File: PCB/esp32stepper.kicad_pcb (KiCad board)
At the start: 4 copper layers, 100 x 80 mm, 117 parts, among them J1 Conn_01x02_Pin, J4 spare, J5 UART0 DEBUG, U1 ESP32-S3-WROOM-2, U2 LDL1117_SOT223, U3 LT8610, U4 74HC595D, U5 USBLC6-2SC6, U6 TCA9548APWR

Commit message: pcb version ready for final check
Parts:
- added ?: , , F.Cu at (200.4, 164.2)
- added ?: , , F.Cu at (198.0, 169.6)
- added ?: , , F.Cu at (190.3, 161.2)
- added ?: , , F.Cu at (198.0, 164.2)
- added ?: , , F.Cu at (205.4, 164.2)
- added ?: , , F.Cu at (200.4, 161.2)
- added ?: , , F.Cu at (190.3, 169.6)
- added ?: , , F.Cu at (198.0, 166.6)
- added ?: , , F.Cu at (190.3, 153.6)
- added ?: , , F.Cu at (198.0, 161.2)
- added ?: , , F.Cu at (200.4, 166.6)
- added ?: , , F.Cu at (200.4, 169.6)
- added ?: , , F.Cu at (202.8, 161.2)
- added ?: , , F.Cu at (202.8, 164.2)
- added C25: 100uF/50V, Capacitor_SMD:CP_Elec_8x10.5, F.Cu at (166.7, 110.5)
- added C26: 100uF/50V, Capacitor_SMD:CP_Elec_8x10.5, F.Cu at (189.6, 110.6)
- added C27: 100uF/50V, Capacitor_SMD:CP_Elec_8x10.5, F.Cu at (215.0, 110.1)
- added C28: 100uF/50V, Capacitor_SMD:CP_Elec_8x10.5, F.Cu at (236.8, 110.4)
- added J6: PWR_SWITCH, Connector_PinHeader_2.54mm:PinHeader_1x03_P2.54mm_Vertical, F.Cu at (242.6, 138.4)
- added NPN1: BC817-40, Package_TO_SOT_SMD:TSOT-23_HandSoldering, F.Cu at (248.2, 144.8)
- added REF**: IEAP_LOGO, VNfootprints:IEAP_LOGO, F.Cu at (212.6, 138.6)
- added fan1: Conn_01x02_Pin, Connector_PinHeader_2.54mm:PinHeader_1x02_P2.54mm_Vertical, F.Cu at (250.9, 122.2)
- moved L2 208.1 mm to (246.0, 151.2), turned to -90 degrees
- moved C13 205.8 mm to (244.1, 146.4), turned to 0 degrees
- moved LED1 205.7 mm to (250.4, 152.6)
- moved C11 205.3 mm to (243.0, 148.9), turned to -90 degrees
- moved R7 204.8 mm to (250.6, 149.2), turned to 0 degrees
- moved C12 204.6 mm to (244.2, 143.1), turned to 180 degrees
- moved USB1 203.3 mm to (251.1, 159.1), turned to 90 degrees
- moved R12 202.6 mm to (250.5, 150.8), turned to 0 degrees
- moved barreljack1 202.4 mm to (242.3, 130.2), turned to 90 degrees
- moved C14 202.3 mm to (239.9, 150.1), turned to 90 degrees
- moved R10 202.2 mm to (243.9, 144.6), turned to 0 degrees
- moved R9 200.4 mm to (241.7, 142.2)
- moved U3 198.7 mm to (239.1, 146.1), turned to 0 degrees
- moved C15 196.9 mm to (240.1, 142.0)
- moved R1 195.1 mm to (244.1, 163.4), turned to 180 degrees
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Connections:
- C15 pad 2: Net-(U3-PG) -> Net-(NPN1-B)
- D3 pad 2: Net-(D3-A) -> PWRSWITCH_diode
- F2 pad 1: Net-(PMOS1-S) -> Net-(PMOS1-D)
- LED1 pad 1: GND -> Net-(LED1-K)
- PMOS1 pad 1: 24Vin -> Net-(PMOS1-D)
- PMOS1 pad 2: Net-(D3-A) -> PWRSWITCH_gate
- PMOS1 pad 3: Net-(PMOS1-S) -> 24Vin
- R12 pad 1: Net-(U3-PG) -> +3V3
- R18 pad 1: Net-(D3-A) -> PWRSWITCH_diode
- R7 pad 2: Net-(U3-PG) -> Net-(NPN1-B)
- U3 pad 15: Net-(U3-PG) -> Net-(NPN1-B)
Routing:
- net +3V3: track 173.0 -> 82.1 mm, vias 22 -> 26
- net endswitch3: track 37.8 -> 74.6 mm, vias 1 -> 2
- net PWRSWITCH_diode: track 0.00 -> 36.0 mm
- net encoder3_SC: track 64.9 -> 32.6 mm, vias 2 -> 0
- net encoder3_SD: track 67.0 -> 35.7 mm, vias 2 -> 0
- net PWRSWITCH_gate: track 0.00 -> 26.8 mm
- net UART: track 150.5 -> 124.9 mm, vias 4 -> 1
- net 24V: track 27.7 -> 50.2 mm
- net Net-(NPN1-B): track 0.00 -> 21.7 mm
- net rx_ext: track 29.7 -> 10.1 mm, vias 1 -> 0
- net reset: track 32.2 -> 12.9 mm
- net step3: track 76.8 -> 57.9 mm
- net tx_ext: track 29.1 -> 10.4 mm, vias 1 -> 0
- net encoder2_SC: track 36.5 -> 18.5 mm, vias 2 -> 0
- net encoder1_SC: track 20.3 -> 37.9 mm
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- added copper zone on B.Cu, net GND
- added copper zone on F.Cu, net GND
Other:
- board text added: "24vin"
- board text added: "diode"
- board text added: "rx"
- board text added: "tx"

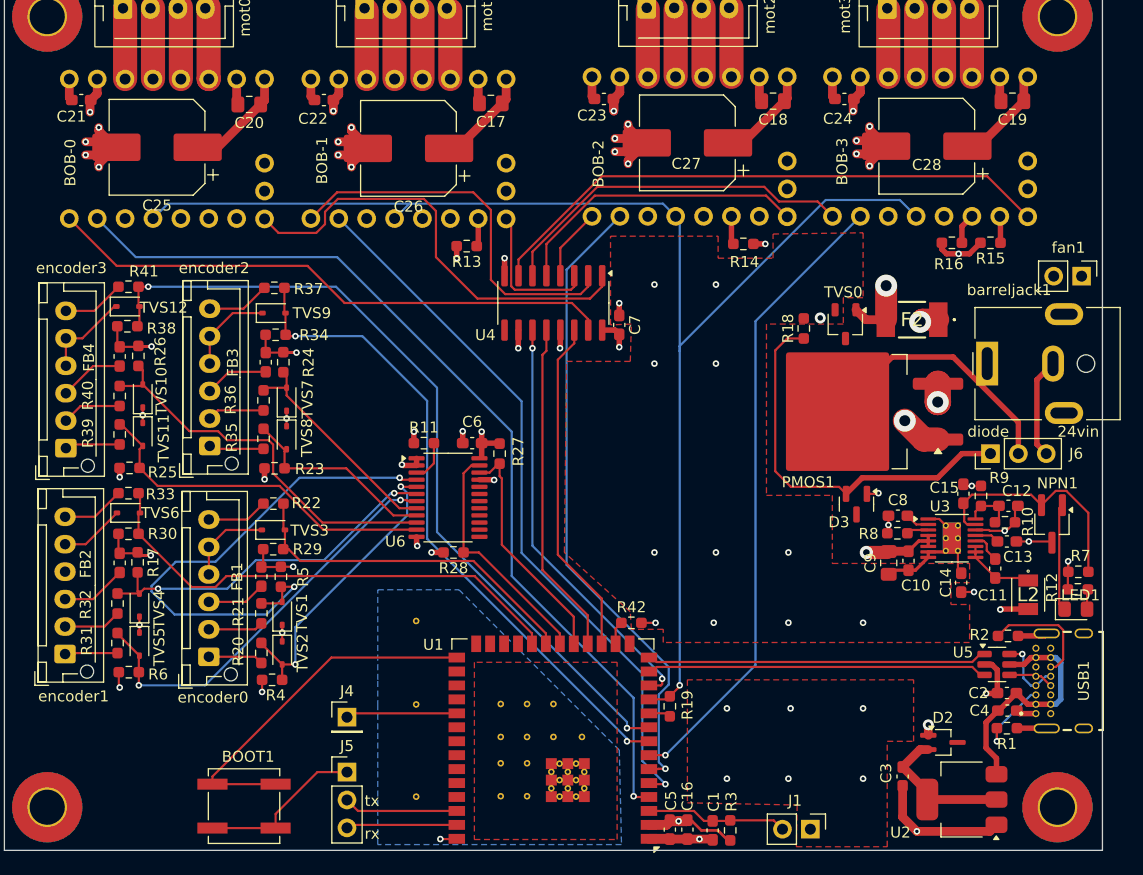
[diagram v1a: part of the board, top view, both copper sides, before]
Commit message: [pcb] Final processing and export of production data
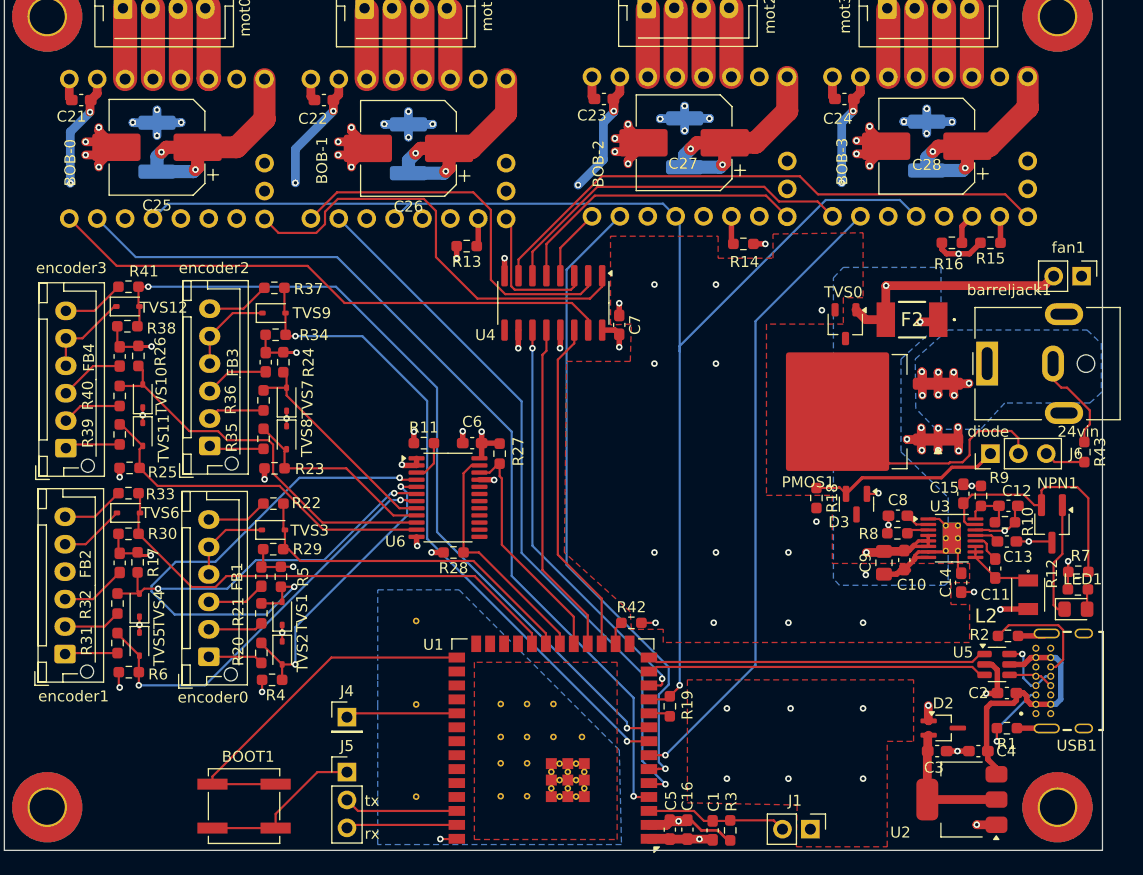
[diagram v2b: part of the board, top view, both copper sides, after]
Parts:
- removed C17, C18, C19, C20: 4u7, Capacitor_SMD:C_0805_2012Metric_Pad1.18x1.45mm_HandSolder
- added F1: Fuse, Fuse:Fuse_1812_4532Metric_Pad1.30x3.40mm_HandSolder, B.Cu at (166.7, 110.5)
- added F3: Fuse, Fuse:Fuse_1812_4532Metric_Pad1.30x3.40mm_HandSolder, B.Cu at (189.6, 110.6)
- added F4: Fuse, Fuse:Fuse_1812_4532Metric_Pad1.30x3.40mm_HandSolder, B.Cu at (214.7, 110.1)
- added F5: Fuse, Fuse:Fuse_1812_4532Metric_Pad1.30x3.40mm_HandSolder, B.Cu at (236.8, 110.4)
- added R43: 100k, Resistor_SMD:R_0603_1608Metric_Pad0.98x0.95mm_HandSolder, F.Cu at (251.1, 138.2)
- moved R18 15.5 mm to (226.7, 142.4), turned to -90 degrees
- moved C4 4.54 mm to (241.5, 165.5), turned to 180 degrees
- moved C3 3.91 mm to (237.7, 165.5), turned to 0 degrees
- moved D2 1.31 mm to (238.3, 163.4)
- moved C9 0.44 mm to (232.9, 148.3)
- moved C10 0.39 mm to (234.7, 148.1)
- moved C27 0.30 mm to (214.7, 110.1)
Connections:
- net Net-(PMOS1-D) renamed 24V_Motor
- BOB-0 pad 16: 24V -> Net-(BOB-0-+VM)
- BOB-1 pad 16: 24V -> Net-(BOB-1-+VM)
- BOB-2 pad 16: 24V -> Net-(BOB-2-+VM)
- BOB-3 pad 16: 24V -> Net-(BOB-3-+VM)
- C25 pad 1: 24V -> Net-(BOB-0-+VM)
- C26 pad 1: 24V -> Net-(BOB-1-+VM)
- C27 pad 1: 24V -> Net-(BOB-2-+VM)
- C28 pad 1: 24V -> Net-(BOB-3-+VM)
- J6 pad 3: 24Vin -> PWRSWITCH_Voltage
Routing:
- net +3V3: track 82.1 -> 112.9 mm, vias 26 -> 30
- net 24V_Motor: track 16.5 -> 41.5 mm, vias 2 -> 24
- net Net-(BOB-0-+VM): track 0.00 -> 21.9 mm, vias 0 -> 2
- net Net-(BOB-3-+VM): track 0.00 -> 21.8 mm, vias 0 -> 2
- net Net-(BOB-1-+VM): track 0.00 -> 21.4 mm, vias 0 -> 2
- net Net-(BOB-2-+VM): track 0.00 -> 20.9 mm, vias 0 -> 2
- net 24V: track 50.2 -> 30.3 mm
- net PWRSWITCH_diode: track 36.0 -> 17.7 mm
- net GND: track 173.7 -> 156.2 mm, vias 52 -> 55
- net PWRSWITCH_Voltage: track 0.00 -> 3.79 mm
- net Net-(NPN1-B): track 21.7 -> 23.5 mm
- net PWRSWITCH_gate: track 26.8 -> 25.1 mm
- net VBUS: track 22.1 -> 23.4 mm
- net /CONN/VO_USB_LDO: track 13.2 -> 12.2 mm
- net Net-(LED1-K): track 9.79 -> 10.6 mm
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- added copper zone on B.Cu, net 24V
- added copper zone on In1.Cu, net 24V_Motor
- added copper zone on B.Cu, net 24Vin
- removed copper zone on In1.Cu, net 24V

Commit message: Auto stash before merge of "main" and "origin/main"
[pcb] Updated main connector and LT8610AC layout
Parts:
- removed ? (x14): , 
- removed REF**: IEAP_LOGO, VNfootprints:IEAP_LOGO
- removed REF**, REF**1, REF**2, REF**3: MountingHole_3.2mm_M3_Pad_TopBottom, MountingHole:MountingHole_3.2mm_M3_Pad_TopBottom
- removed barreljack1: PWR, Connector_BarrelJack:BarrelJack_CUI_PJ-063AH_Horizontal
- added H5: MountingHole_Pad, MountingHole:MountingHole_3.2mm_M3_DIN965_Pad, F.Cu at (156.9, 170.5)
- added H6: MountingHole_Pad, MountingHole:MountingHole_3.2mm_M3_DIN965_Pad, F.Cu at (248.9, 170.5)
- added H7: MountingHole_Pad, MountingHole:MountingHole_3.2mm_M3_DIN965_Pad, F.Cu at (156.9, 99.0)
- added H8: MountingHole_Pad, MountingHole:MountingHole_3.2mm_M3_DIN965_Pad, F.Cu at (248.9, 99.0)
- added J2: Barrel_Jack_Switch_Pin3Ring, Connector_BarrelJack:BarrelJack_Wuerth_6941xx301002, F.Cu at (241.9, 131.0)
- added R44: 100k, Resistor_SMD:R_0603_1608Metric_Pad0.98x0.95mm_HandSolder, B.Cu at (243.4, 134.0)
- added R45: 100k, Resistor_SMD:R_0603_1608Metric_Pad0.98x0.95mm_HandSolder, B.Cu at (247.4, 134.0)
- moved L2 5.64 mm to (240.4, 151.0)
- moved C14 2.69 mm to (237.4, 151.0)
- moved C11 0.49 mm to (243.4, 148.5)
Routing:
- net Net-(J2-Pad2): track 0.00 -> 4.86 mm
- net PWRSWITCH_gate: track 25.1 -> 29.6 mm, vias 0 -> 1
- net 24Vin: track 33.9 -> 36.6 mm
- net GND: track 156.2 -> 154.1 mm, vias 55 -> 56
- net +3V3: track 112.9 -> 113.9 mm, vias 30 -> 29
- added copper zone on F.Cu, net 24Vin
